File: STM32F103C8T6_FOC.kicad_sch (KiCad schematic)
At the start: 1 part

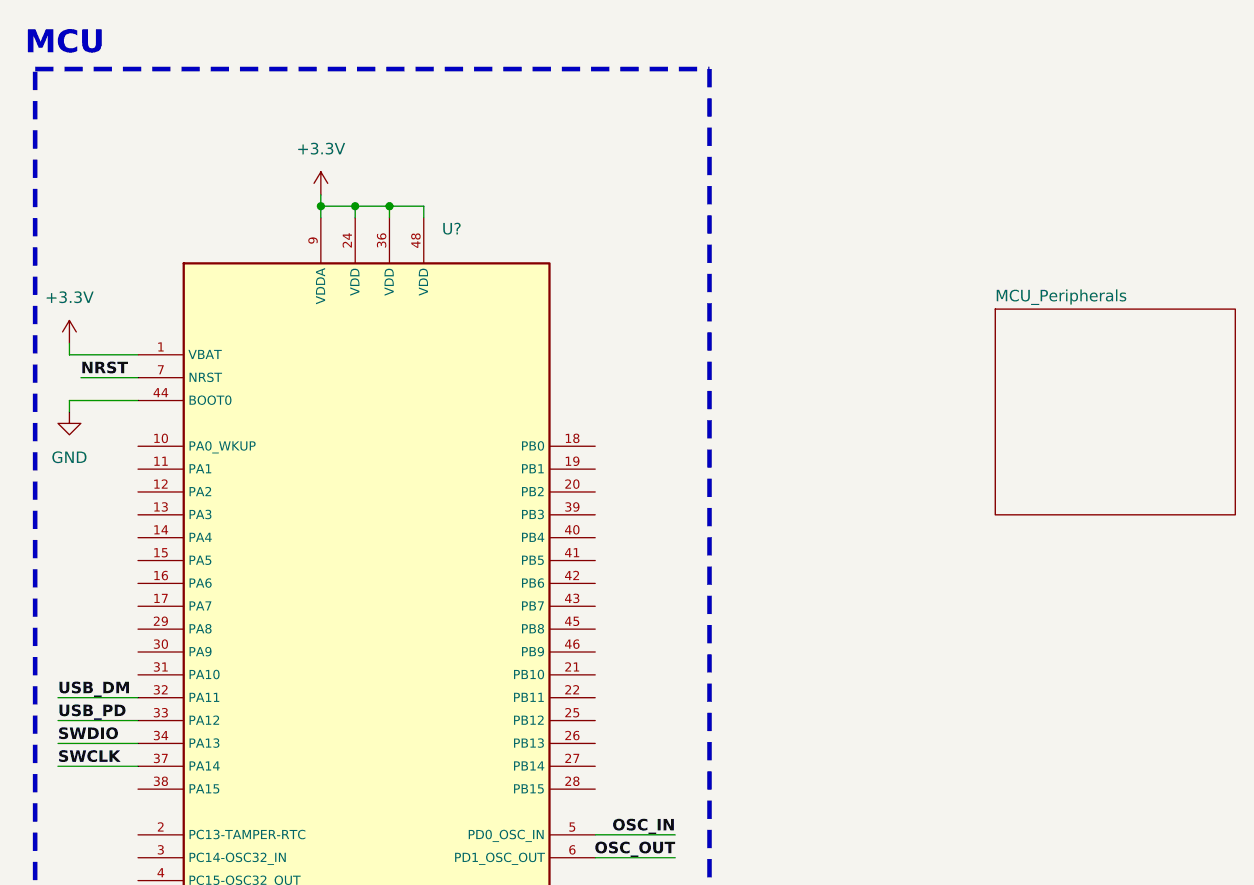
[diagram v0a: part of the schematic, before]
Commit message: Power Rail Update
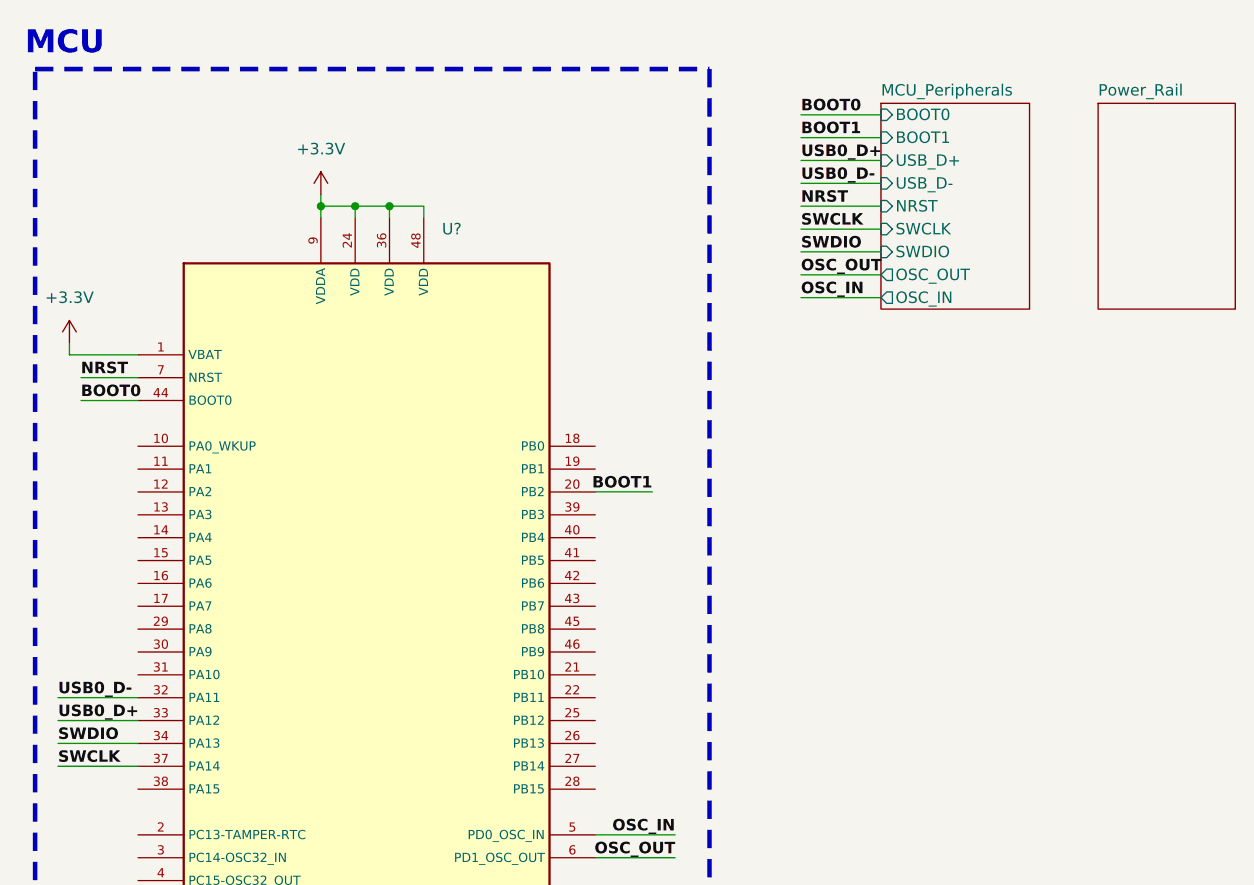
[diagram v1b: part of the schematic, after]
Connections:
- net GND: no longer U?.44 (BOOT0)
- net BOOT1: now reaches U?.20 (PB2)
- net USB_DM renamed USB0_D-
- net USB_PD renamed USB0_D+
- new net BOOT0: U?.44 (BOOT0)
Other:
- added sheet Power_Rail (Power_Rail.kicad_sch)
- sheet MCU_Peripherals ports: added BOOT0, BOOT1, NRST, OSC_IN, OSC_OUT, SWCLK, SWDIO, USB_D+, USB_D-; removed none

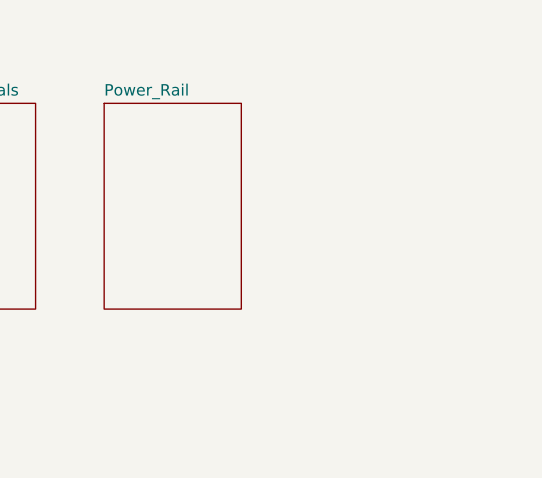
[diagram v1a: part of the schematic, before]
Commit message: TMC2209 Update
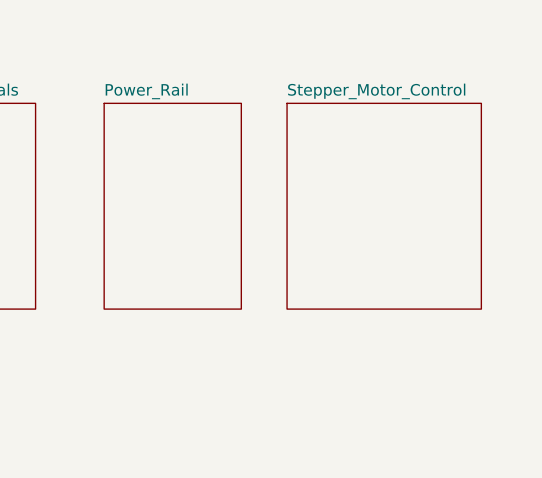
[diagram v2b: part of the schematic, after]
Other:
- added sheet Stepper_Motor_Control (Stepper_Motor_Control.kicad_sch)
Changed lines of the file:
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@@
+		)
+	)
+	(sheet
+		(at 156.21 21.59)
+		(size 21.59 22.86)
+		(fields_autoplaced yes)
+		(stroke
+			(width 0.1524)
+			(type solid)
+		)
+		(fill
+			(color 0 0 0 0.0000)
+		)
+		(property "Sheetname" "Stepper_Motor_Control"
+			(at 156.21 20.8784 0)
+			(effects
+				(font
+					(size 1.27 1.27)
+				)
+				(justify left bottom)
+			)
+		)
+		(property "Sheetfile" "Stepper_Motor_Control.kicad_sch"
+			(at 156.21 45.0346 0)
+			(effects
+				(font
+					(size 1.27 1.27)
+				)
+				(justify left top)
+				(hide yes)
+			)
+		)
+		(instances
+			(project "STM32F103C8T6_FOC"
+				(path "/d228dd74-472e-4320-b112-509b57639e8e"
+					(page "4")
+				)
+			)
 		)
 	)

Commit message: Stepper Motor Control Update
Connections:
- net SCL: now reaches U?.42 (PB6)
- net SDA: now reaches U?.43 (PB7)
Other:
- sheet MCU_Peripherals ports: added SCL, SDA; removed none
- sheet Stepper_Motor_Control ports: added AS5600_SCL, AS5600_SDA, DIAG, DIR, STEP, UART_RX, UART_TX; removed none
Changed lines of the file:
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@@
+	(wire
+		(pts
+			(xy 80.01 74.93) (xy 86.36 74.93)
+		)
+		(stroke
+			(width 0)
+			(type default)
+		)
+	)
 	(wire
 		(pts
@@
 	(wire
 		(pts
+			(xy 80.01 77.47) (xy 86.36 77.47)
+		)
+		(stroke
+			(width 0)
+			(type default)
+		)
+	)
+	(wire
+		(pts
 			(xy 49.53 31.75) (xy 49.53 33.02)
 		)
@@
 	(wire
 		(pts
+			(xy 111.76 45.72) (xy 102.87 45.72)
+		)
+		(stroke
+			(width 0)
+			(type default)
+		)
+	)
+	(wire
+		(pts
 			(xy 53.34 34.29) (xy 53.34 33.02)
 		)
@@
 		(pts
 			(xy 80.01 64.77) (xy 86.36 64.77)
+		)
+		(stroke
+			(width 0)
+			(type default)
+		)
+	)
+	(wire
+		(pts
+			(xy 111.76 48.26) (xy 102.87 48.26)
 		)
 		(stroke
@@
 		)
 	)
+	(label "SDA"
+		(at 102.87 48.26 0)
+		(effects
+			(font
+				(size 1.27 1.27)
+				(thickness 0.254)
+				(bold yes)
+			)
+			(justify left bottom)
+		)
+	)
 	(label "SWDIO"
 		(at 20.32 92.71 0)
@@
 		)
 	)
+	(label "SCL"
+		(at 102.87 45.72 0)
+		(effects
+			(font
+				(size 1.27 1.27)
+				(thickness 0.254)
+				(bold yes)
+			)
+			(justify left bottom)
+		)
+	)
 	(label "NRST"
 		(at 22.86 52.07 0)
@@
 		)
 	)
+	(label "SCL"
+		(at 86.36 74.93 180)
+		(effects
+			(font
+				(size 1.27 1.27)
+				(thickness 0.254)
+				(bold yes)
+			)
+			(justify right bottom)
+		)
+	)
 	(label "USB0_D-"
 		(at 102.87 30.48 0)
@@
 	(label "BOOT1"
 		(at 86.36 64.77 180)
+		(effects
+			(font
+				(size 1.27 1.27)
+				(thickness 0.254)
+				(bold yes)
+			)
+			(justify right bottom)
+		)
+	)
+	(label "SDA"
+		(at 86.36 77.47 180)
 		(effects
 			(font
@@
 	(sheet
 		(at 111.76 21.59)
-		(size 16.51 22.86)
+		(size 16.51 27.94)
 		(fields_autoplaced yes)
 		(stroke
@@
 		)
 		(property "Sheetfile" "MCU_Peripherals.kicad_sch"
-			(at 111.76 45.0346 0)
+			(at 111.76 50.1146 0)
 			(effects
 				(font
@@
 		(pin "OSC_IN" output
 			(at 111.76 43.18 180)
+			(effects
+				(font
+					(size 1.27 1.27)
+				)
+				(justify left)
+			)
+		)
+		(pin "SCL" passive
+			(at 111.76 45.72 180)
+			(effects
+				(font
+					(size 1.27 1.27)
+				)
+				(justify left)
+			)
+		)
+		(pin "SDA" passive
+			(at 111.76 48.26 180)
 			(effects
 				(font
@@
 	)
 	(sheet
-		(at 156.21 21.59)
-		(size 21.59 22.86)
+		(at 111.76 53.34)
+		(size 21.59 17.78)
 		(fields_autoplaced yes)
 		(stroke
@@
 		)
 		(property "Sheetname" "Stepper_Motor_Control"
-			(at 156.21 20.8784 0)
+			(at 111.76 52.6284 0)
 			(effects
 				(font
@@
 		)
 		(property "Sheetfile" "Stepper_Motor_Control.kicad_sch"
-			(at 156.21 45.0346 0)
+			(at 111.76 71.7046 0)
 			(effects
 				(font
@@
 			)
 		)
+		(pin "UART_RX" bidirectional
+			(at 111.76 54.61 180)
+			(effects
+				(font
+					(size 1.27 1.27)
+				)
+				(justify left)
+			)
+		)
+		(pin "UART_TX" bidirectional
+			(at 111.76 57.15 180)
+			(effects
+				(font
+					(size 1.27 1.27)
+				)
+				(justify left)
+			)
+		)
+		(pin "DIAG" bidirectional
+			(at 111.76 59.69 180)
+			(effects
+				(font
+					(size 1.27 1.27)
+				)
+				(justify left)
+			)
+		)
+		(pin "STEP" bidirectional
+			(at 111.76 62.23 180)
+			(effects
+				(font
+					(size 1.27 1.27)
+				)
+				(justify left)
+			)
+		)
+		(pin "DIR" bidirectional
+			(at 111.76 64.77 180)
+			(effects
+				(font
+					(size 1.27 1.27)
+				)
+				(justify left)
+			)
+		)
+		(pin "AS5600_SDA" bidirectional
+			(at 111.76 67.31 180)
+			(effects
+				(font
+					(size 1.27 1.27)
+				)
+				(justify left)
+			)
+		)
+		(pin "AS5600_SCL" bidirectional
+			(at 111.76 69.85 180)
+			(effects
+				(font
+					(size 1.27 1.27)
+				)
+				(justify left)
+			)
+		)

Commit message: CAN & EEPROM Update
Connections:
- net UART2_TX: now reaches U?.12 (PA2)
- net UART2_RX: now reaches U?.13 (PA3)
- net CAN_TX: now reaches U?.29 (PA8)
- net CAN_RX: now reaches U?.30 (PA9)
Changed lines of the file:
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@@
+	(wire
+		(pts
+			(xy 19.05 67.31) (xy 29.21 67.31)
+		)
+		(stroke
+			(width 0)
+			(type default)
+		)
+	)
 	(wire
 		(pts
@@
 	(wire
 		(pts
+			(xy 19.05 64.77) (xy 29.21 64.77)
+		)
+		(stroke
+			(width 0)
+			(type default)
+		)
+	)
+	(wire
+		(pts
 			(xy 102.87 25.4) (xy 111.76 25.4)
 		)
@@
 	(wire
 		(pts
+			(xy 20.32 82.55) (xy 29.21 82.55)
+		)
+		(stroke
+			(width 0)
+			(type default)
+		)
+	)
+	(wire
+		(pts
 			(xy 80.01 77.47) (xy 86.36 77.47)
 		)
@@
 		(pts
 			(xy 49.53 31.75) (xy 49.53 33.02)
+		)
+		(stroke
+			(width 0)
+			(type default)
+		)
+	)
+	(wire
+		(pts
+			(xy 20.32 80.01) (xy 29.21 80.01)
 		)
 		(stroke
@@
 		)
 	)
+	(label "UART2_TX"
+		(at 19.05 64.77 0)
+		(effects
+			(font
+				(size 1.27 1.27)
+				(thickness 0.254)
+				(bold yes)
+			)
+			(justify left bottom)
+		)
+	)
 	(label "SWDIO"
 		(at 20.32 92.71 0)
@@
 		)
 	)
+	(label "UART2_RX"
+		(at 19.05 67.31 0)
+		(effects
+			(font
+				(size 1.27 1.27)
+				(thickness 0.254)
+				(bold yes)
+			)
+			(justify left bottom)
+		)
+	)
 	(label "NRST"
 		(at 22.86 52.07 0)
@@
 		)
 	)
+	(label "CAN_RX"
+		(at 20.32 82.55 0)
+		(effects
+			(font
+				(size 1.27 1.27)
+				(thickness 0.254)
+				(bold yes)
+			)
+			(justify left bottom)
+		)
+	)
 	(label "OSC_OUT"
 		(at 102.87 40.64 0)
@@
 		)
 	)
+	(label "CAN_TX"
+		(at 20.32 80.01 0)
+		(effects
+			(font
+				(size 1.27 1.27)
+				(thickness 0.254)
+				(bold yes)
+			)
+			(justify left bottom)
+		)
+	)

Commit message: LEDs, Button & Small fixes
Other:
- sheet MCU_Peripherals ports: added B_LED, CAN_RX, CAN_TX, G_LED, R_LED, SCL_EEPROM, SDA_EEPROM, U_BUTTON, WC_EEPROM; removed none

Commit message: Schematic finish & ERC
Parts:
- gave numbers to parts that had none: 1
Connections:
- net STEP: now reaches U1.18 (PB0)
- net WC_EEPROM: now reaches U1.21 (PB10)
- net DIAG: now reaches U1.22 (PB11)
- net DIR: now reaches U1.25 (PB12)
- net G_LED: now reaches U1.26 (PB13)
- net B_LED: now reaches U1.27 (PB14)
- net R_LED: now reaches U1.28 (PB15)
- net U_BUTTON: now reaches U1.46 (PB9)
- no-connect marks 0 -> 16

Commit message: Layout Update
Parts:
- added H1, H2, H3, H4: MountingHole_Pad, MountingHole:MountingHole_3.2mm_M3_ISO7380_Pad, symbol Mechanical:MountingHole_Pad
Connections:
- net BOOT0 is gone; now on net GND: U1.44 (BOOT0)
- net GND: now also H1.1, H2.1, H3.1, H4.1
- net WC_EEPROM: now also U1.39 (PB3); no longer U1.21 (PB10)
- net BOOT1: no longer names the net of U1.20 (PB2)
- no-connect marks 16 -> 17
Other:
- sheet MCU_Peripherals ports: added none; removed BOOT0, BOOT1
- note added: "PCB_MOUNT"

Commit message: Layout Update
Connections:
- net B_LED: now also U1.40 (PB4); no longer U1.27 (PB14)
- net G_LED: now also U1.41 (PB5); no longer U1.26 (PB13)
- net R_LED: now also U1.39 (PB3); no longer U1.28 (PB15)
- net U_BUTTON: now also U1.27 (PB14); no longer U1.46 (PB9)
- net WC_EEPROM: now also U1.38 (PA15); no longer U1.39 (PB3)
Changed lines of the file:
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@@
-	)
-	(no_connect
-		(at 80.01 69.85)
 	)
 	(no_connect
@@
 	)
 	(no_connect
-		(at 80.01 72.39)
-	)
-	(no_connect
 		(at 29.21 59.69)
 	)
 	(no_connect
+		(at 80.01 92.71)
+	)
+	(no_connect
+		(at 80.01 82.55)
+	)
+	(no_connect
 		(at 80.01 62.23)
 	)
@@
 	)
 	(no_connect
+		(at 80.01 97.79)
+	)
+	(no_connect
 		(at 29.21 62.23)
 	)
@@
 		(at 80.01 80.01)
 	)
-	(no_connect
-		(at 29.21 97.79)
-	)
 	(wire
 		(pts
@@
 	(wire
 		(pts
-			(xy 80.01 97.79) (xy 88.9 97.79)
+			(xy 80.01 67.31) (xy 88.9 67.31)
 		)
 		(stroke
@@
 	(wire
 		(pts
-			(xy 80.01 67.31) (xy 92.71 67.31)
+			(xy 29.21 97.79) (xy 16.51 97.79)
 		)
 		(stroke
@@
 	(wire
 		(pts
-			(xy 80.01 92.71) (xy 88.9 92.71)
+			(xy 80.01 72.39) (xy 88.9 72.39)
 		)
 		(stroke
@@
 	(wire
 		(pts
-			(xy 80.01 82.55) (xy 92.71 82.55)
+			(xy 80.01 95.25) (xy 92.71 95.25)
 		)
 		(stroke
@@
 	(wire
 		(pts
-			(xy 80.01 95.25) (xy 88.9 95.25)
+			(xy 80.01 69.85) (xy 88.9 69.85)
 		)
 		(stroke
@@
 	)
 	(rectangle
-		(start 17.78 17.78)
+		(start 15.24 17.78)
 		(end 93.98 137.16)
 		(stroke
@@
 	)
 	(label "WC_EEPROM"
-		(at 92.71 67.31 180)
-		(effects
-			(font
-				(size 1.27 1.27)
-				(thickness 0.254)
-				(bold yes)
-			)
-			(justify right bottom)
+		(at 16.51 97.79 0)
+		(effects
+			(font
+				(size 1.27 1.27)
+				(thickness 0.254)
+				(bold yes)
+			)
+			(justify left bottom)
 		)
 	)
 	(label "U_BUTTON"
-		(at 92.71 82.55 180)
+		(at 92.71 95.25 180)
 		(effects
 			(font
@@
 	)
 	(label "G_LED"
-		(at 88.9 92.71 180)
+		(at 88.9 72.39 180)
 		(effects
 			(font
@@
 	)
 	(label "R_LED"
-		(at 88.9 97.79 180)
+		(at 88.9 67.31 180)
 		(effects
 			(font
@@
 	)
 	(label "B_LED"
-		(at 88.9 95.25 180)
-		(effects
-			(font
+		(at 88.9 69.85 180)
+		(effects
+			(font
